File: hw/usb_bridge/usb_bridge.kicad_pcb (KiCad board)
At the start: 2 copper layers, 51 x 31 mm, 70 parts, among them J1 USB_C_Receptacle_USB2.0_14P, J2 DE9, J3 SWD, J4 BOOT, U1 CH340E, U2 MAX485E, U3 CH334R, U4 74LVC2G04, U5 MCP1754S-3302xCB, U6 TJA1051T-3, U7 STM32G0B1CBT, Y1 HCI XC53G2-12.000-F20LJDT, Y2 HCI XC53G2-8.000-F12NJHP

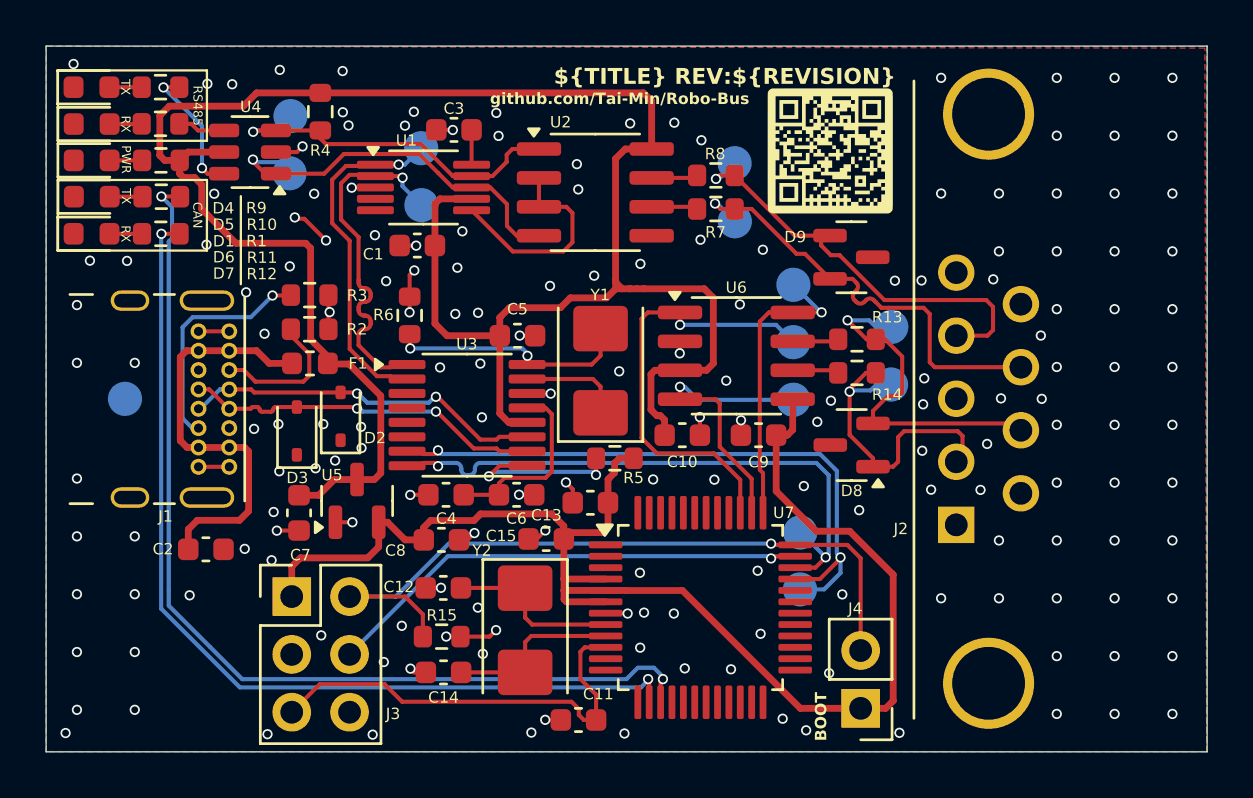
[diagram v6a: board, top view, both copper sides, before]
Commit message: Add LED jumper
Signed-off-by: Mateusz Pająk <22417805+Tai-Min@users.noreply.github.com>
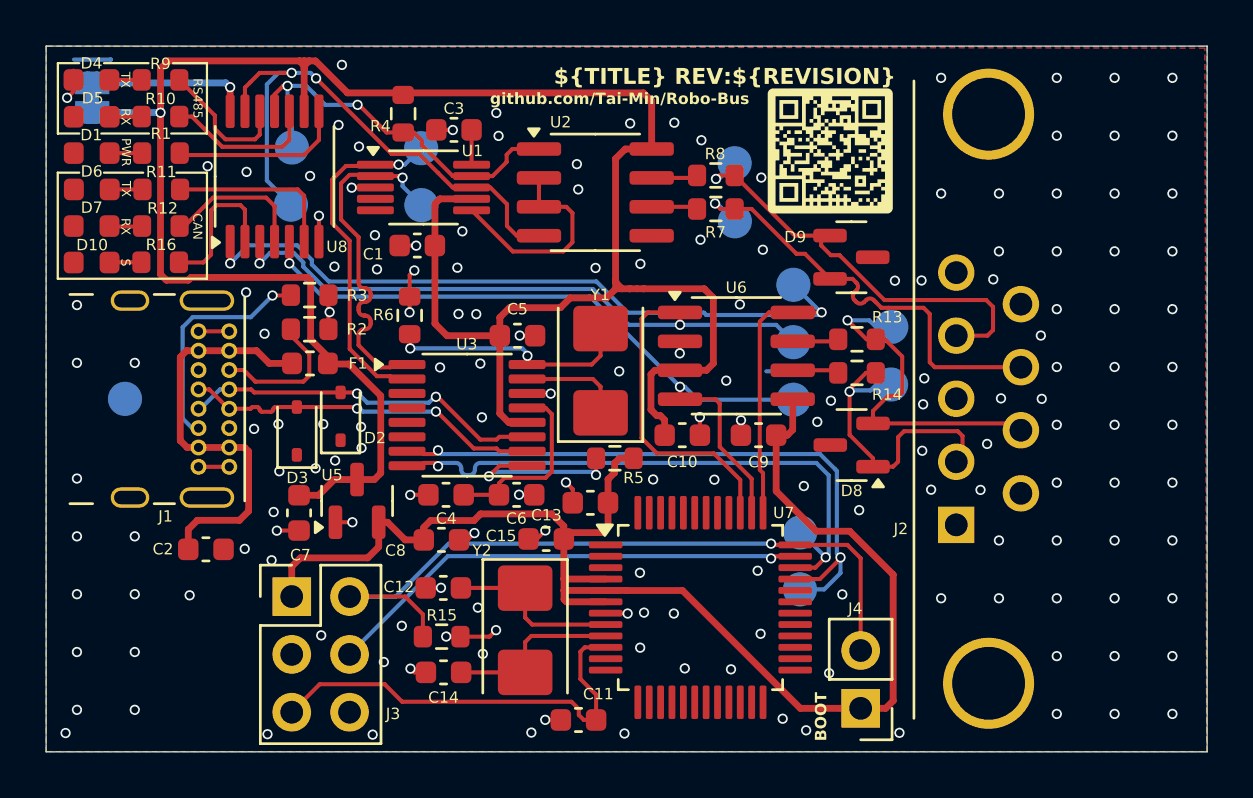
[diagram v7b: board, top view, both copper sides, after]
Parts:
- removed U4: 74LVC2G04, Package_TO_SOT_SMD:SOT-23-6
- added D10: yellow, LED_SMD:LED_0603_1608Metric, F.Cu at (128.5, 96.0)
- added JP1: Jumper_2_Bridged, Jumper:SolderJumper-2_P1.3mm_Bridged_RoundedPad1.0x1.5mm, B.Cu at (128.5, 88.8)
- added R16: 1K, Resistor_SMD:R_0603_1608Metric, F.Cu at (131.5, 96.0)
- added U8: 74HC04, Package_SO:TSSOP-14_4.4x5mm_P0.65mm, F.Cu at (136.5, 92.3)
- moved R4 3.64 mm to (142.1, 89.5)
- moved TP10 1.38 mm to (137.2, 93.5)
- moved TP11 1.38 mm to (137.2, 91.0)
- moved D7 0.34 mm to (128.5, 94.5)
- moved R12 0.34 mm to (131.5, 94.5)
- moved D1 0.32 mm to (128.5, 91.2)
- moved D4 0.32 mm to (128.4, 88.0)
- moved D5 0.32 mm to (128.5, 89.7)
- moved D6 0.32 mm to (128.5, 92.8)
- moved R1 0.32 mm to (131.5, 91.2)
- moved R10 0.32 mm to (131.5, 89.6)
- moved R11 0.32 mm to (131.5, 92.8)
- moved R9 0.32 mm to (131.5, 88.0)
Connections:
- net /mcu/CAN_RX renamed /C_RX
- net /mcu/CAN_S renamed /C_S
- net /mcu/CAN_TX renamed /C_TX
- R1 pad 2: +5V -> Net-(R1-Pad2)
- R11 pad 2: /mcu/LED_TX -> Net-(R11-Pad2)
- R12 pad 2: /mcu/LED_RX -> Net-(R12-Pad2)
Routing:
- net /mcu/LED_TX: track 43.6 -> 0.00 mm, vias 2 -> 0
- net /mcu/LED_RX: track 41.7 -> 0.00 mm, vias 2 -> 0
- net /C_S: track 13.7 -> 42.4 mm, vias 1 -> 2
- net /C_TX: track 19.9 -> 40.9 mm, vias 1 -> 2
- net /C_RX: track 13.4 -> 33.8 mm, vias 1 -> 2
- net /RS_TX: track 16.9 -> 24.8 mm, vias 1 -> 2
- net Net-(R1-Pad2): track 0.00 -> 7.69 mm
- net Net-(R11-Pad2): track 0.00 -> 7.59 mm
- net +5V: track 95.8 -> 103.3 mm, vias 0 -> 1
- net /LED_PWR: track 0.00 -> 7.20 mm, vias 0 -> 1
- net Net-(R16-Pad2): track 0.00 -> 6.85 mm
- net Net-(R12-Pad2): track 0.00 -> 6.77 mm
- net Net-(R10-Pad2): track 2.09 -> 6.77 mm
- net GND: track 28.1 -> 31.0 mm, vias 176 -> 167
- net /RS_RX: track 16.2 -> 17.7 mm, vias 1 -> 2
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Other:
- board text added: "LED_PWR"

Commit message: Add 5V TP, Cleanup
Signed-off-by: Mateusz Pająk <22417805+Tai-Min@users.noreply.github.com>
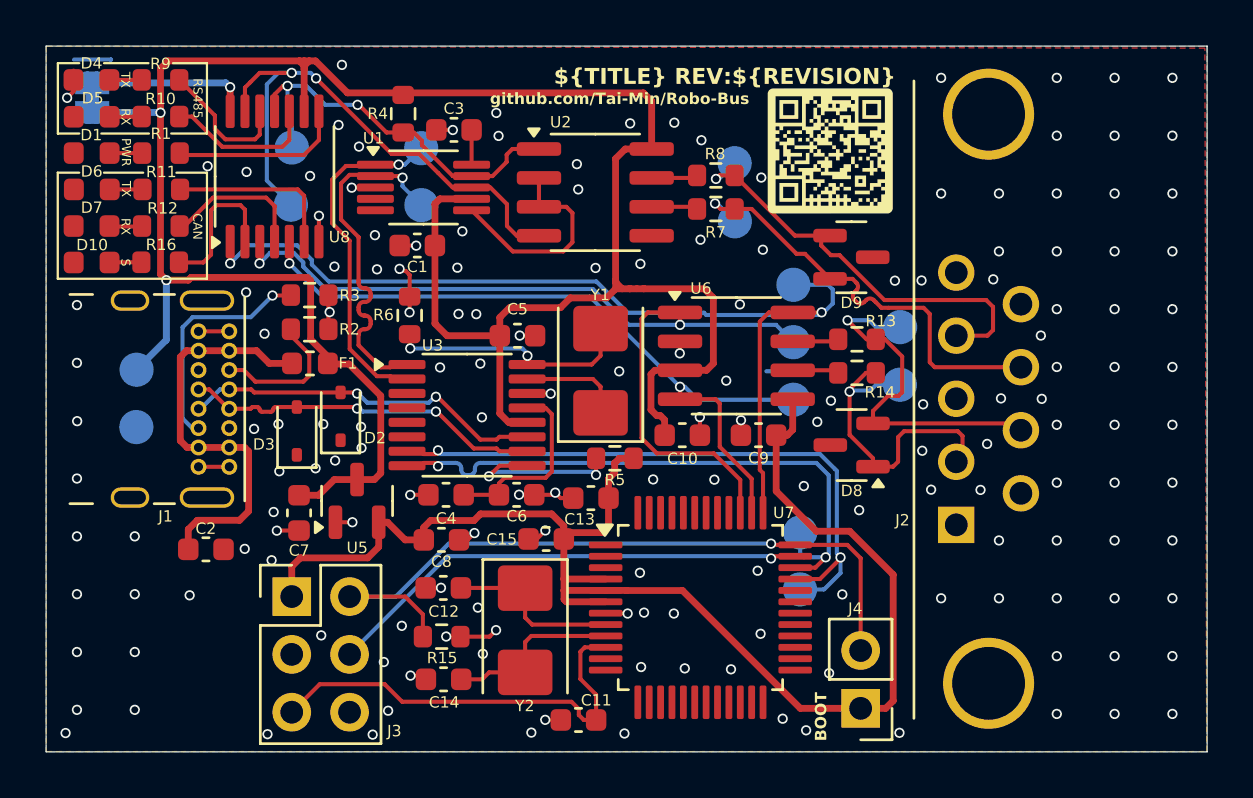
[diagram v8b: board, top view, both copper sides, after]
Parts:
- added TP2: TestPoint, TestPoint:TestPoint_Pad_D1.5mm, B.Cu at (130.4, 100.8)
- moved TP1 1.34 mm to (130.4, 103.3)
- moved TP16 0.39 mm to (164.0, 101.4)
- moved TP15 0.39 mm to (164.0, 98.9)
- moved C14 0.31 mm to (143.9, 114.4)
- moved C13 0.21 mm to (150.4, 106.4)
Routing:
- net +5V: track 103.3 -> 107.8 mm, vias 1 -> 2
- net /C_S: track 42.4 -> 43.8 mm
- net GND: track 31.0 -> 32.4 mm
- net /CAN+: track 14.8 -> 15.9 mm
- net /CAN-: track 13.4 -> 14.4 mm
- net /D_CAN+: track 26.2 -> 26.8 mm
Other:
- board text added: "5V"
